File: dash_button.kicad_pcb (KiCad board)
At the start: 2 copper layers, 200 x 28 mm, 55 parts, among them J1 1050570001, J2 MINI 5PTP, J3 Debug, J4 JST PH 1x2, J5 JST PH 1x5, P1 CONN_02X03, Q1 AO3401A, Q2 AO3401A, Q3 AO3401A, Q4 AO3401A, Q5 AO3401A, Q6 AO3401A, SW1 SW_Push, SW2 SW_Push, SW3 SW_Push, SW4 SW_Push, SW5 SW_Push, U1 ATtiny441-M, U2 HT7550-1

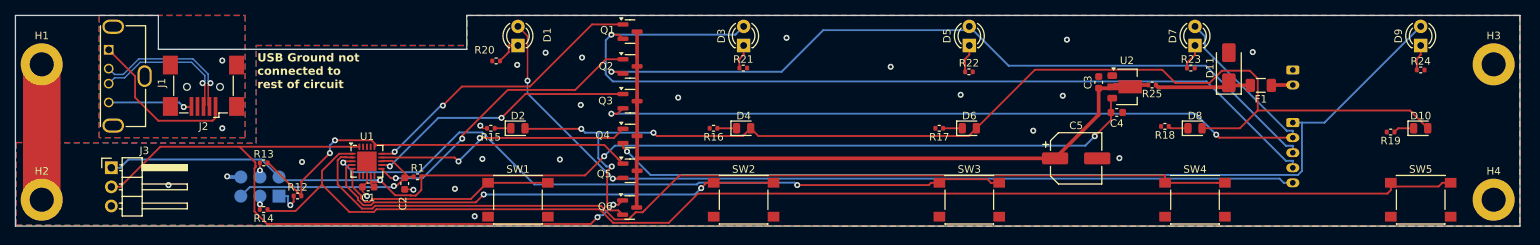
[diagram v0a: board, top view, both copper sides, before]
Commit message: add automation for generating board_files
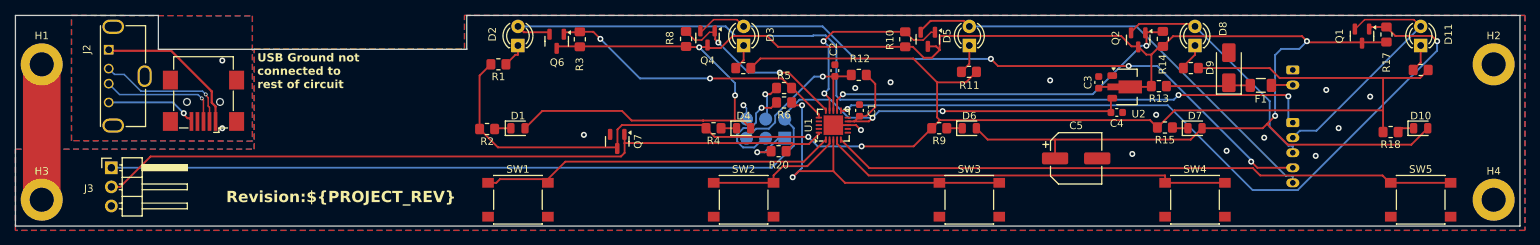
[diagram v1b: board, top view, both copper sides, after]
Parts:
- removed Q5: AO3401A, Package_TO_SOT_SMD:SOT-23
- added Q7: AO3400A, Package_TO_SOT_SMD:SOT-23, F.Cu at (115.0, 63.8)
- added R10: 10k, Resistor_SMD:R_0805_2012Metric_Pad1.20x1.40mm_HandSolder, F.Cu at (153.3, 50.2)
- added R14: 10k, Resistor_SMD:R_0805_2012Metric_Pad1.20x1.40mm_HandSolder, F.Cu at (187.5, 50.1)
- added R17: 10k, Resistor_SMD:R_0805_2012Metric_Pad1.20x1.40mm_HandSolder, F.Cu at (217.2, 49.5)
- added R3: 10k, Resistor_SMD:R_0805_2012Metric_Pad1.20x1.40mm_HandSolder, F.Cu at (110.0, 50.2)
- added R8: 10k, Resistor_SMD:R_0805_2012Metric_Pad1.20x1.40mm_HandSolder, F.Cu at (124.2, 50.1)
- R1: renamed from R20; footprint Resistor_SMD:R_0402_1005Metric -> Resistor_SMD:R_0805_2012Metric_Pad1.20x1.40mm_HandSolder
- R11: renamed from R22; footprint Resistor_SMD:R_0402_1005Metric -> Resistor_SMD:R_0805_2012Metric_Pad1.20x1.40mm_HandSolder
- R12: renamed from R1; footprint Resistor_SMD:R_0402_1005Metric -> Resistor_SMD:R_0805_2012Metric_Pad1.20x1.40mm_HandSolder
- R13: renamed from R25; value 1k -> 10; footprint Resistor_SMD:R_0402_1005Metric -> Resistor_SMD:R_0805_2012Metric_Pad1.20x1.40mm_HandSolder
- R15: renamed from R18; footprint Resistor_SMD:R_0402_1005Metric -> Resistor_SMD:R_0805_2012Metric_Pad1.20x1.40mm_HandSolder
- R16: renamed from R23; footprint Resistor_SMD:R_0402_1005Metric -> Resistor_SMD:R_0805_2012Metric_Pad1.20x1.40mm_HandSolder
- R18: renamed from R19; footprint Resistor_SMD:R_0402_1005Metric -> Resistor_SMD:R_0805_2012Metric_Pad1.20x1.40mm_HandSolder
- R19: renamed from R24; footprint Resistor_SMD:R_0402_1005Metric -> Resistor_SMD:R_0805_2012Metric_Pad1.20x1.40mm_HandSolder
- R2: renamed from R15; footprint Resistor_SMD:R_0402_1005Metric -> Resistor_SMD:R_0805_2012Metric_Pad1.20x1.40mm_HandSolder
- R20: renamed from R12; footprint Resistor_SMD:R_0402_1005Metric -> Resistor_SMD:R_0805_2012Metric_Pad1.20x1.40mm_HandSolder
- R4: renamed from R16; footprint Resistor_SMD:R_0402_1005Metric -> Resistor_SMD:R_0805_2012Metric_Pad1.20x1.40mm_HandSolder
- R5: renamed from R13; footprint Resistor_SMD:R_0402_1005Metric -> Resistor_SMD:R_0805_2012Metric_Pad1.20x1.40mm_HandSolder
- R6: renamed from R14; footprint Resistor_SMD:R_0402_1005Metric -> Resistor_SMD:R_0805_2012Metric_Pad1.20x1.40mm_HandSolder
- R7: renamed from R21; footprint Resistor_SMD:R_0402_1005Metric -> Resistor_SMD:R_0805_2012Metric_Pad1.20x1.40mm_HandSolder
- R9: renamed from R17; footprint Resistor_SMD:R_0402_1005Metric -> Resistor_SMD:R_0805_2012Metric_Pad1.20x1.40mm_HandSolder
- moved Q1 97.3 mm to (214.0, 49.8), turned to -90 degrees
- moved R6 70.6 mm to (137.2, 58.6)
- moved R5 69.9 mm to (137.2, 56.6)
- moved P1 67.7 mm to (134.7, 62.0)
- moved Q2 67.6 mm to (184.2, 50.2), turned to -90 degrees
- moved C1 66.1 mm to (147.2, 59.6), turned to 90 degrees
- moved R20 64.2 mm to (136.4, 65.0)
- moved U1 62.2 mm to (143.7, 61.6), turned to 90 degrees
- moved R12 60.2 mm to (147.1, 54.9)
- moved C2 59.1 mm to (143.9, 54.3), turned to 90 degrees
- moved Q3 40.4 mm to (156.3, 50.2), turned to -90 degrees
- moved Q6 24.1 mm to (107.0, 50.4), turned to -90 degrees
- moved Q4 16.6 mm to (127.0, 50.0), turned to -90 degrees
- moved J1 2.00 mm to (60.0, 58.5)
- moved R13 0.92 mm to (187.0, 56.4)
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- renumbered D2 to D1, D9 to D11, D1 to D2, D8 to D7, D7 to D8, D11 to D9, H3 to H2, H2 to H3, J2 to J1, J1 to J2
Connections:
- D1 pad 2: Net-(D10-A) -> +BATT
- D10 pad 2: Net-(D10-A) -> +BATT
- D11 pad 2: /DRN_LOK_R -> /out_pas_seat
- D2 pad 2: /DRN_DRV_SEAT -> /out_drv_seat
- D3 pad 2: /DRN_PAS_SEAT -> /out_lock_f
- D4 pad 2: Net-(D10-A) -> +BATT
- D5 pad 2: /DRN_SW_LIGHTS -> /out_lock_r
- D6 pad 2: Net-(D10-A) -> +BATT
- D7 pad 2: Net-(D10-A) -> +BATT
- D8 pad 2: /DRN_LOK_F -> /out_lights
- J3 pad 2: Net-(J3-Pin_2) -> /TXD_PWM
- J5 pad 1: /DRN_LOK_R -> /out_drv_seat
- J5 pad 2: /DRN_LOK_F -> /out_pas_seat
- J5 pad 3: /DRN_SW_LIGHTS -> /out_lights
- J5 pad 4: /DRN_PAS_SEAT -> /out_lock_f
- J5 pad 5: /DRN_DRV_SEAT -> /out_lock_r
- Q1 pad 2: /DRN_PAS_SEAT -> /out_pas_seat
- Q2 pad 1: /GATE_SW_LIGHTS -> /GATE_LIGHTS
- Q2 pad 2: /DRN_SW_LIGHTS -> /out_lights
- Q3 pad 1: /GATE_LOK_F -> /GATE_LOK_R
- Q3 pad 2: /DRN_LOK_F -> /out_lock_r
- Q4 pad 1: /GATE_LOK_R -> /GATE_LOK_F
- Q4 pad 2: /DRN_LOK_R -> /out_lock_f
- Q6 pad 1: Net-(J3-Pin_2) -> /gate_drv_seat
- Q6 pad 2: Net-(D10-A) -> /out_drv_seat
- R1 pad 2: GND -> Net-(Q7-D)
- R11 pad 2: GND -> Net-(Q7-D)
- R15 pad 2: GND -> Net-(Q7-D)
- R16 pad 2: GND -> Net-(Q7-D)
- R18 pad 2: GND -> Net-(Q7-D)
- R19 pad 2: GND -> Net-(Q7-D)
- R2 pad 2: GND -> Net-(Q7-D)
- R20 pad 2: /GATE_DRV_SEAT -> /TXD_PWM
- R4 pad 2: GND -> Net-(Q7-D)
- R5 pad 2: /GATE_DRV_SEAT -> /gate_drv_seat
- R7 pad 2: GND -> Net-(Q7-D)
- R9 pad 2: GND -> Net-(Q7-D)
- SW2 pad 1: /SW_PAS_SEAT -> /SW_LOK_F
- SW3 pad 1: /SW_LIGHTS -> /SW_LOK_R
- SW4 pad 1: /SW_LOK_F -> /SW_LIGHTS
- SW5 pad 1: /SW_LOK_R -> /SW_PAS_SEAT
- U1 pad 1: /SW_LOK_R -> /SW_DRV_SEAT
- U1 pad 11: /GATE_SW_LIGHTS -> /GATE_PAS_SEAT
- U1 pad 12: /GATE_LOK_F -> /GATE_LIGHTS
- U1 pad 15: /GATE_PAS_SEAT -> /GATE_LOK_F
- U1 pad 16: /GATE_DRV_SEAT -> /gate_drv_seat
- U1 pad 20: Net-(J3-Pin_2) -> /TXD_PWM
- U1 pad 3: /SW_LIGHTS -> /SW_LOK_R
- U1 pad 4: /SW_PAS_SEAT -> /SW_LIGHTS
- U1 pad 5: /SW_DRV_SEAT -> /SW_PAS_SEAT
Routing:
- net Net-(Q7-D): track 0.00 -> 213.2 mm, vias 0 -> 2
- net Net-(D10-A): track 154.1 -> 0.00 mm, vias 3 -> 0
- net +BATT: track 105.1 -> 254.5 mm, vias 0 -> 4
- net /SW_LOK_R: track 171.0 -> 44.2 mm, vias 0 -> 2
- net /DRN_PAS_SEAT: track 122.4 -> 0.00 mm, vias 1 -> 0
- net /DRN_LOK_R: track 121.3 -> 0.00 mm, vias 1 -> 0
- net /out_drv_seat: track 0.00 -> 119.0 mm, vias 0 -> 2
- net /DRN_DRV_SEAT: track 117.5 -> 0.00 mm, vias 2 -> 0
- net /DRN_LOK_F: track 114.4 -> 0.00 mm, vias 2 -> 0
- net /SW_LOK_F: track 128.9 -> 18.7 mm
- net /DRN_SW_LIGHTS: track 102.3 -> 0.00 mm, vias 1 -> 0
- net /TXD_PWM: track 0.00 -> 100.7 mm
- net Net-(J3-Pin_2): track 95.7 -> 0.00 mm, vias 2 -> 0
- net /out_lock_f: track 0.00 -> 87.7 mm, vias 0 -> 3
- net /GATE_PAS_SEAT: track 39.2 -> 102.9 mm
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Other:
- board text added: "Revision:${PROJECT_REV}"

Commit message: use nchannel mosfet + pchannel mosfet
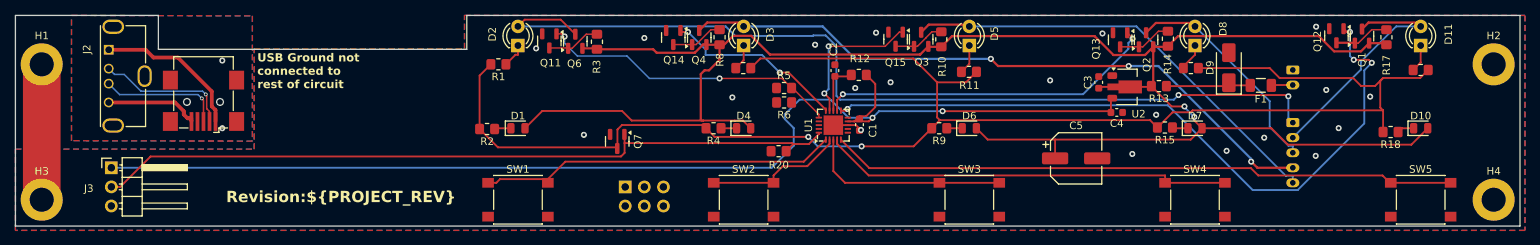
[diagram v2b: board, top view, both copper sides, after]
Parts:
- added Q11: AO3400A, Package_TO_SOT_SMD:SOT-23, F.Cu at (106.0, 50.4)
- added Q12: AO3400A, Package_TO_SOT_SMD:SOT-23, F.Cu at (210.6, 49.7)
- added Q13: AO3400A, Package_TO_SOT_SMD:SOT-23, F.Cu at (181.8, 50.2)
- added Q14: AO3400A, Package_TO_SOT_SMD:SOT-23, F.Cu at (122.5, 49.9)
- added Q15: AO3400A, Package_TO_SOT_SMD:SOT-23, F.Cu at (152.0, 50.2)
- P1: footprint project:programmer-pads -> Connector_PinHeader_2.54mm:PinHeader_2x03_P2.54mm_Vertical
- moved P1 20.2 mm to (116.1, 69.8), turned to -90 degrees
- moved R10 4.79 mm to (158.1, 50.2)
- moved R8 4.46 mm to (128.6, 49.9)
- moved Q6 2.47 mm to (109.4, 50.4), turned to 90 degrees
- moved R3 2.30 mm to (112.3, 50.5)
- moved C1 1.90 mm to (147.2, 61.5), turned to -90 degrees
- moved Q4 1.10 mm to (125.9, 49.9), turned to 90 degrees
- moved Q2 1.05 mm to (185.3, 50.2), turned to 90 degrees
- moved Q3 0.88 mm to (155.4, 50.2), turned to 90 degrees
- moved R14 0.68 mm to (188.2, 50.1)
- moved R17 0.36 mm to (217.2, 49.9)
- turned Q1 to 90 degrees
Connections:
- Q1 pad 1: /GATE_PAS_SEAT -> Net-(Q1-G)
- Q1 pad 2: /out_pas_seat -> +BATT
- Q1 pad 3: +BATT -> /out_pas_seat
- Q2 pad 1: /GATE_LIGHTS -> Net-(Q13-D)
- Q2 pad 2: /out_lights -> +BATT
- Q2 pad 3: +BATT -> /out_lights
- Q3 pad 1: /GATE_LOK_R -> Net-(Q15-D)
- Q3 pad 2: /out_lock_r -> +BATT
- Q3 pad 3: +BATT -> /out_lock_r
- Q4 pad 1: /GATE_LOK_F -> Net-(Q14-D)
- Q4 pad 2: /out_lock_f -> +BATT
- Q4 pad 3: +BATT -> /out_lock_f
- Q6 pad 1: /gate_drv_seat -> Net-(Q11-D)
- Q6 pad 2: /out_drv_seat -> +BATT
- Q6 pad 3: +BATT -> /out_drv_seat
- R10 pad 2: /GATE_LOK_R -> Net-(Q15-D)
- R14 pad 2: /GATE_LIGHTS -> Net-(Q13-D)
- R17 pad 2: /GATE_PAS_SEAT -> Net-(Q1-G)
- R3 pad 2: /gate_drv_seat -> Net-(Q11-D)
- R6 pad 1: /SW_LOK_R -> /SW_DRV_SEAT
- R8 pad 2: /GATE_LOK_F -> Net-(Q14-D)
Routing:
- net /SW_LOK_R: track 44.2 -> 26.9 mm, vias 2 -> 0
- net /RESET: track 22.5 -> 7.01 mm, vias 1 -> 0
- net /SCK: track 13.3 -> 0.00 mm, vias 1 -> 0
- net +BATT: track 254.5 -> 244.2 mm, vias 4 -> 2
- net /GATE_PAS_SEAT: track 102.9 -> 94.2 mm, vias 2 -> 4
- net Net-(Q1-G): track 0.00 -> 7.41 mm
- net Net-(Q13-D): track 0.00 -> 7.21 mm
- net Net-(Q11-D): track 0.00 -> 7.12 mm
- net Net-(Q14-D): track 0.00 -> 6.97 mm
- net Net-(Q15-D): track 0.00 -> 6.89 mm
- net /GATE_LOK_R: track 26.3 -> 19.7 mm
- net /MISO: track 6.34 -> 0.00 mm, vias 1 -> 0
- net /MOSI: track 5.33 -> 0.00 mm, vias 1 -> 0
- net /out_drv_seat: track 119.0 -> 123.2 mm
- net /GATE_LIGHTS: track 49.7 -> 45.6 mm
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
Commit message: Move JST connectors to center
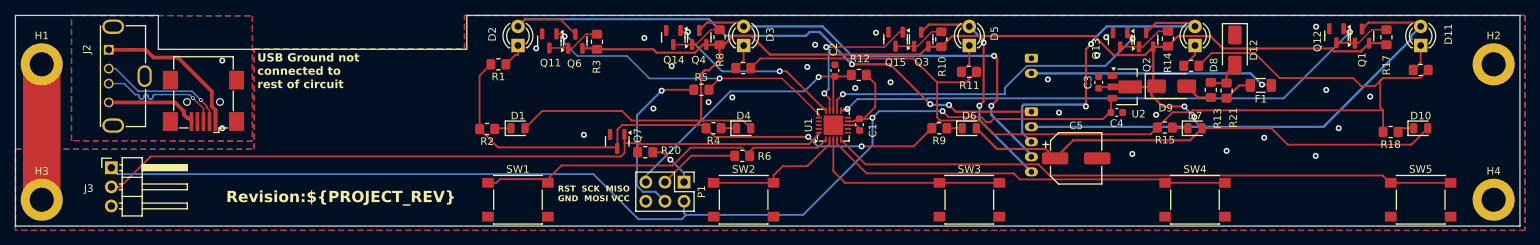
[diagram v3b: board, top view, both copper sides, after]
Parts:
- added D12: SMAJ16A, Diode_SMD:D_SMA, F.Cu at (197.1, 51.6)
- added R21: 4.7, Resistor_SMD:R_0805_2012Metric_Pad1.20x1.40mm_HandSolder, F.Cu at (196.0, 57.0)
- D9: value SMAJ16CA -> SS34
- P1: moved to F.Cu
- R13: value 10 -> 4.7
- moved J4 34.8 mm to (170.1, 52.7)
- moved J5 34.8 mm to (170.1, 59.8)
- moved R20 17.7 mm to (118.7, 65.2), turned to 180 degrees
- moved R5 11.0 mm to (126.2, 56.9)
- moved R6 9.02 mm to (131.6, 65.7)
- moved D9 7.99 mm to (188.7, 56.4), turned to 0 degrees
- moved P1 7.85 mm to (123.9, 69.2)
- moved R13 6.92 mm to (193.9, 56.9), turned to -90 degrees
- moved R16 0.30 mm to (191.3, 53.7)
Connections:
- D9 pad 1: Net-(D9-A1) -> +BATT
- D9 pad 2: GND -> Net-(D9-A)
- F1 pad 2: Net-(D9-A1) -> Net-(F1-Pad2)
- R13 pad 1: Net-(D9-A1) -> Net-(D12-A2)
- R13 pad 2: +BATT -> Net-(D9-A)
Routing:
- net /out_drv_seat: track 123.2 -> 83.0 mm, vias 2 -> 3
- net /out_pas_seat: track 32.1 -> 65.9 mm
- net /RESET: track 7.01 -> 38.4 mm, vias 0 -> 1
- net /out_lock_f: track 87.5 -> 57.6 mm, vias 3 -> 2
- net Net-(J4-Pin_2): track 2.87 -> 32.6 mm, vias 0 -> 1
- net /out_lock_r: track 59.1 -> 30.1 mm, vias 0 -> 2
- net /MOSI: track 0.00 -> 22.9 mm, vias 0 -> 1
- net /GATE_PAS_SEAT: track 94.2 -> 73.0 mm, vias 4 -> 2
- net /out_lights: track 29.7 -> 44.7 mm, vias 0 -> 2
- net Net-(D9-A1): track 11.5 -> 0.00 mm
- net /SCK: track 0.00 -> 10.7 mm
- net /MISO: track 0.00 -> 6.49 mm, vias 0 -> 1
- net Net-(D12-A2): track 0.00 -> 5.00 mm
- net Net-(F1-Pad2): track 0.00 -> 3.85 mm
- net Net-(D9-A): track 0.00 -> 3.82 mm
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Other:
- board text added: "RST SCK MISO GND MOSI VCC"

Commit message: fixup BOM
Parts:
- C5: value 330u -> 100u
- SW1, SW2, SW3, SW4, SW5: value SW_Push -> TS-1002S-08526C
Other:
- board text added: "Revision:rev3-dirty"
- board text removed: "Revision:${PROJECT_REV}"

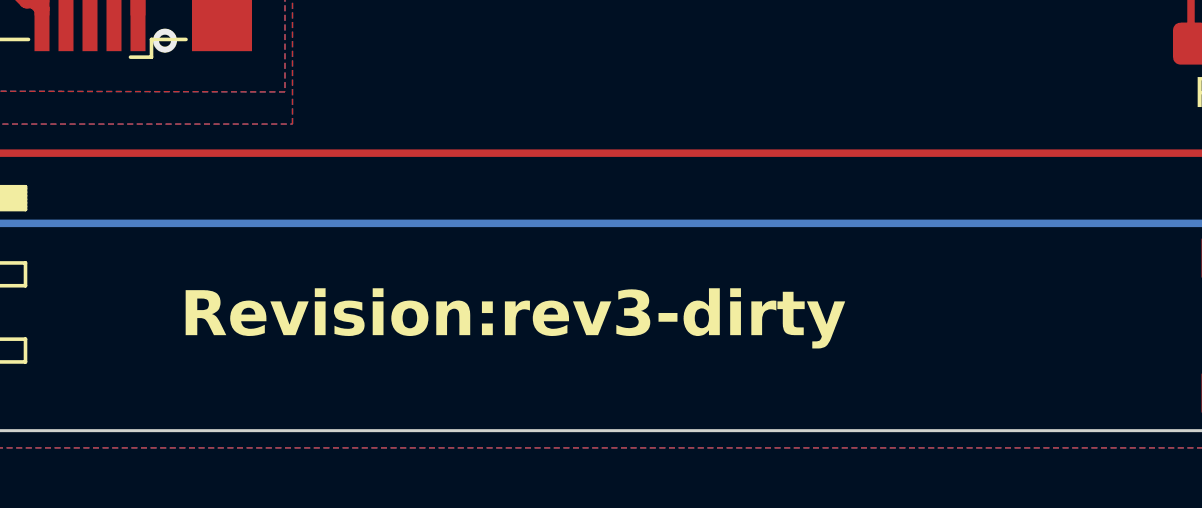
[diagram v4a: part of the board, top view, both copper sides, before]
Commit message: build_files.py generates for pcbway
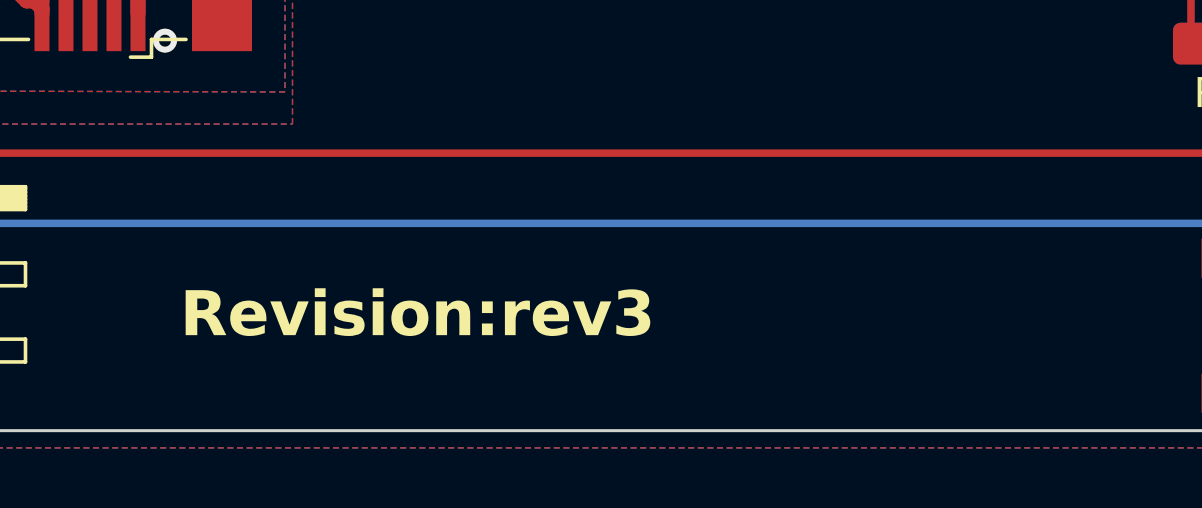
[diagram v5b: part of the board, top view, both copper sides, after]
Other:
- board text added: "Revision:rev3"
- board text removed: "Revision:rev3-dirty"
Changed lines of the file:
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@@
 		(layer "Edge.Cuts")
 	)
-	(gr_text "Revision:rev3-dirty"
+	(gr_text "Revision:rev3"
 		(at 63 72 0)
 		(layer "F.SilkS")

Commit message: Change Attiny part number to attiny441-mur
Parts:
- U1: value ATtiny441-M -> ATtiny441-MUR
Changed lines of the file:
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@@
 			)
 		)
-		(property "Value" "ATtiny441-M"
+		(property "Value" "ATtiny441-MUR"
 			(at 0 3.3 -90)
 			(layer "F.Fab")
@@
 			)
 		)
-		(property "PartNo" "ATTINY441-MUR"
-			(at 0 0 90)
-			(unlocked yes)
-			(layer "F.Fab")
-			(hide yes)
-			(effects
-				(font
-					(size 1 1)
-					(thickness 0.15)
-				)
-			)
-		)
 		(property "Manufacturer" "ATMEL"
 			(at 0 0 90)
@@
 			)
 		)
-		(property "MPN" "ATTINY441-MMH"
+		(property "MPN" "ATTINY441-MUR"
 			(at 0 0 90)
 			(unlocked yes)
